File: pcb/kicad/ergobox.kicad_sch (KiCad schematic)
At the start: 1 part

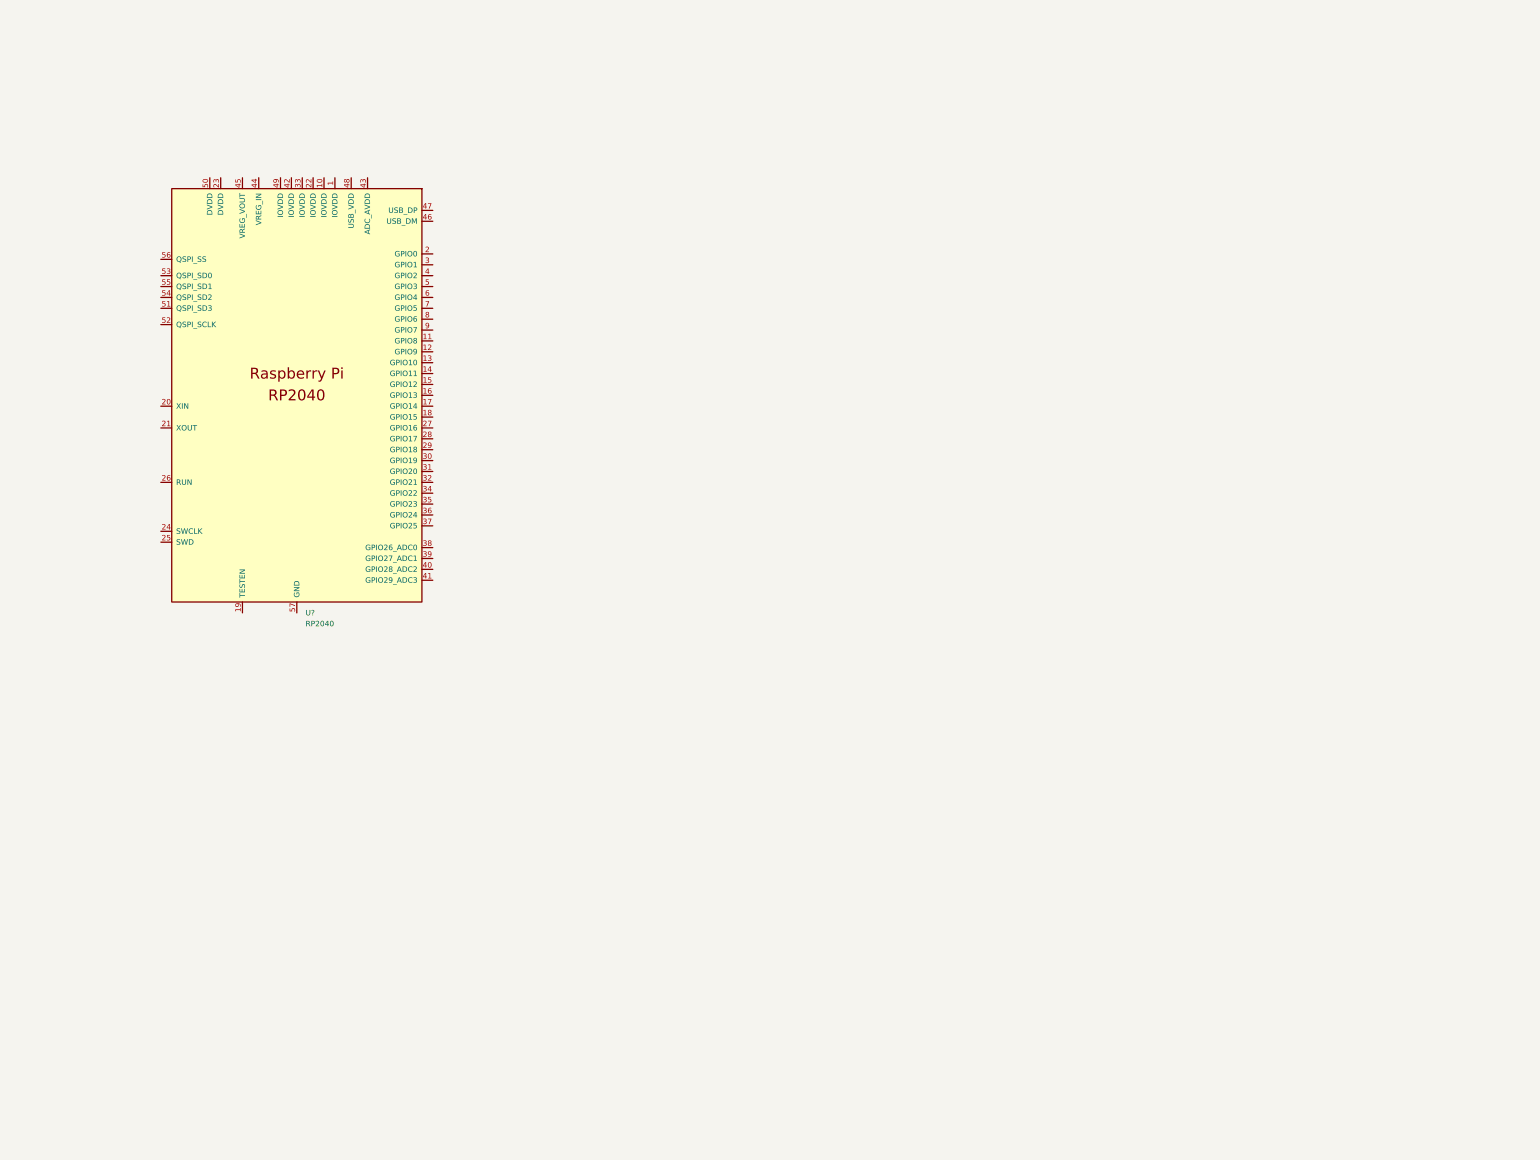
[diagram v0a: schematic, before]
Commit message: feat: adds initial schematic design
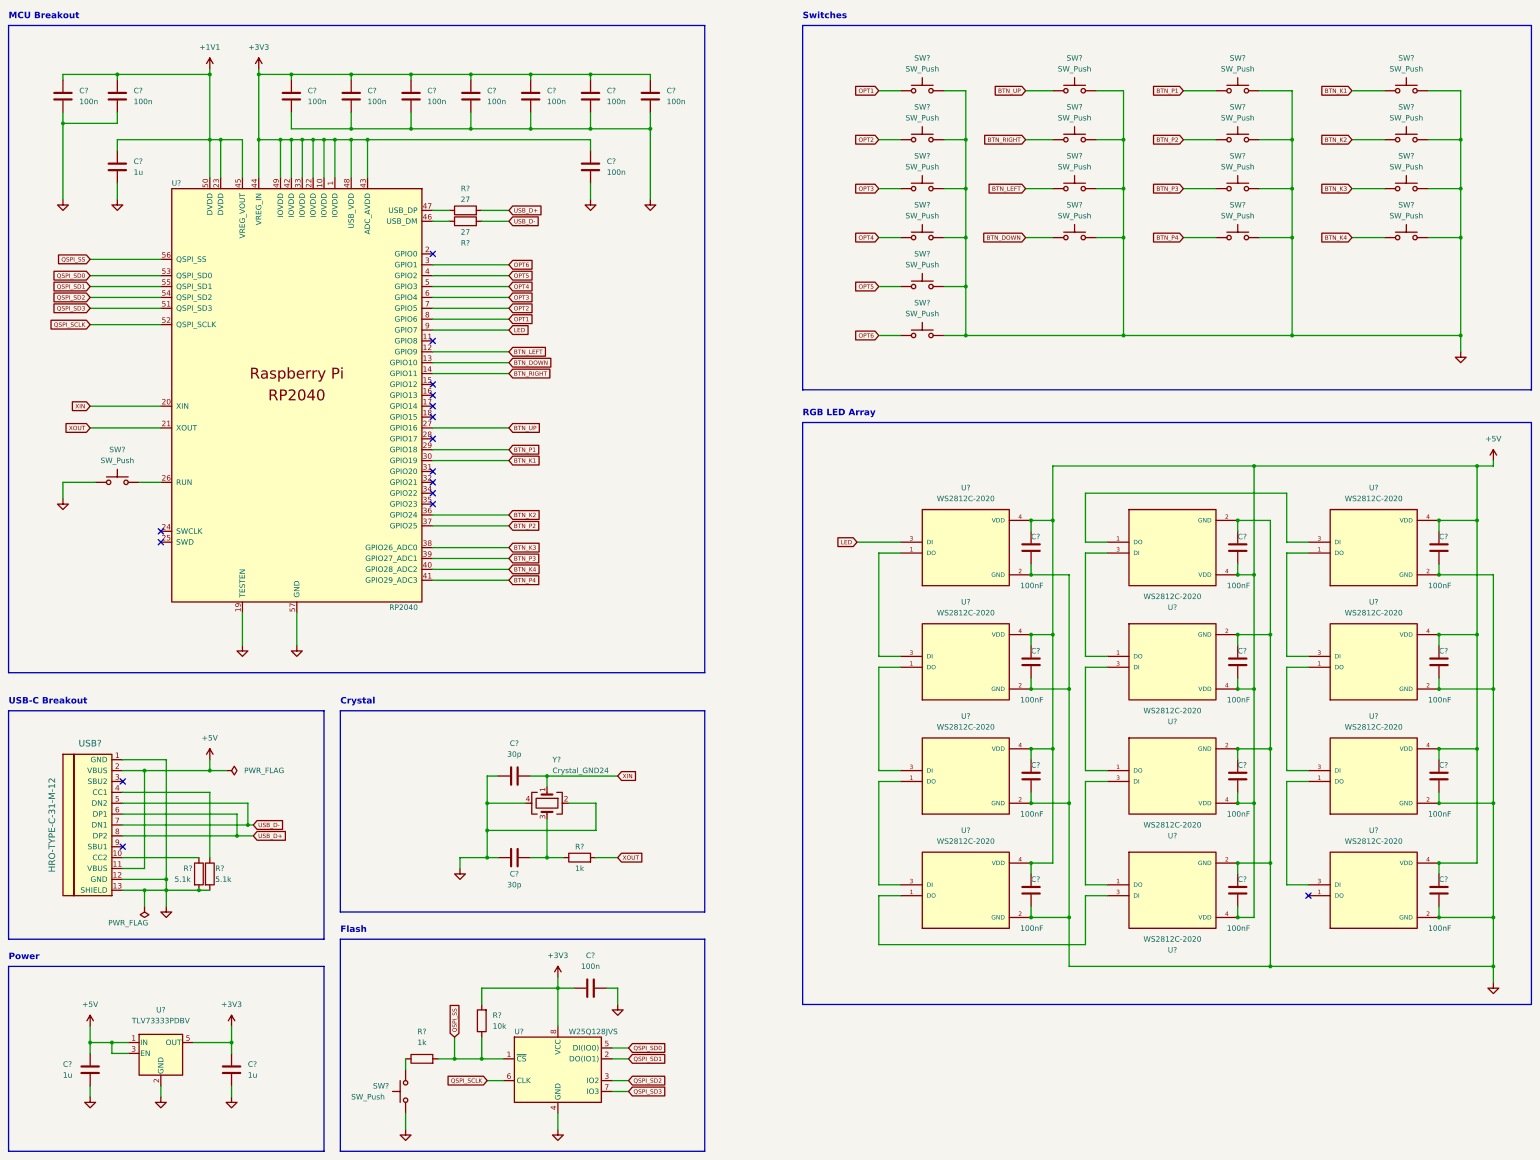
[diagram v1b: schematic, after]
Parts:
- added C? (x11): 100n, symbol Device:C
- added C? (x12): 100nF, symbol Device:C
- added C? (x3): 1u, symbol Device:C
- added C? (x2): 30p, symbol Device:C
- added R? (x2): 5.1k, symbol Device:R
- added R? (x2): 1k, symbol Device:R
- added R?: 10k, symbol Device:R
- added R? (x2): 27, symbol Device:R
- added SW? (x20): SW_Push, symbol Switch:SW_Push
- added U? (x12): WS2812C-2020, LED_WS2812C-2020, symbol WS2812C-2020:WS2812C-2020
- added U?: W25Q128JVS, Package_SO:SOIC-8_5.23x5.23mm_P1.27mm, symbol Memory_Flash:W25Q128JVS
- added U?: TLV73333PDBV, Package_TO_SOT_SMD:SOT-23-5, symbol Regulator_Linear:TLV73333PDBV
- added USB?: HRO-TYPE-C-31-M-12, symbol USB-C:HRO-TYPE-C-31-M-12
- added Y?: Crystal_GND24, symbol Device:Crystal_GND24
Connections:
- net +3V3: now reaches U?.1 (IOVDD)
- net +3V3: now also U?.10 (IOVDD), U?.22 (IOVDD), U?.33 (IOVDD), U?.42 (IOVDD), U?.43 (ADC_AVDD), U?.44 (VREG_IN), U?.48 (USB_VDD), U?.49 (IOVDD), C?.1, C?.1, C?.1, C?.1, C?.1, C?.1, C?.1, C?.1, C?.1, C?.1, R?.2, U?.5 (OUT), U?.8 (VCC)
- net BTN_LEFT: now reaches U?.12 (GPIO9)
- net BTN_LEFT: now also SW?.1
- net BTN_DOWN: now reaches U?.13 (GPIO10)
- net BTN_DOWN: now also SW?.1
- net BTN_RIGHT: now reaches U?.14 (GPIO11)
- net BTN_RIGHT: now also SW?.1
- net GND: now reaches U?.19 (TESTEN)
- net GND: now also U?.57 (GND), C?.1, C?.1, C?.1, C?.1, C?.1, C?.1, C?.2, C?.2, C?.2, C?.2, C?.2, C?.2, C?.2, C?.2, C?.2, C?.2, C?.2, C?.2, C?.2, C?.2, C?.2, C?.2, C?.2, C?.2, C?.2, C?.2, C?.2, C?.2, R?.2, R?.2, SW?.1, SW?.1, SW?.2, SW?.2, SW?.2, SW?.2, SW?.2, SW?.2, SW?.2, SW?.2, SW?.2, SW?.2, SW?.2, SW?.2, SW?.2, SW?.2, SW?.2, SW?.2, SW?.2, SW?.2, U?.2 (GND), U?.2 (GND), U?.2 (GND), U?.2 (GND), U?.2 (GND), U?.2 (GND), U?.2 (GND), U?.2 (GND), U?.2 (GND), U?.2 (GND), U?.2 (GND), U?.2 (GND), U?.2 (GND), U?.4 (GND), USB?.1 (GND), USB?.12 (GND), USB?.13 (SHIELD), Y?.2, Y?.4
- net XIN: now reaches U?.20 (XIN)
- net XIN: now also C?.2, Y?.1
- net XOUT: now reaches U?.21 (XOUT)
- net XOUT: now also R?.2
- net +1V1: now reaches U?.23 (DVDD)
- net +1V1: now also U?.45 (VREG_VOUT), U?.50 (DVDD), C?.1, C?.1, C?.1
- net at U?.26 (RUN): now also SW?.2
- net BTN_UP: now reaches U?.27 (GPIO16)
- net BTN_UP: now also SW?.1
- net BTN_P1: now reaches U?.29 (GPIO18)
- net BTN_P1: now also SW?.1
- net OPT6: now reaches U?.3 (GPIO1)
- net OPT6: now also SW?.1
- net BTN_K1: now reaches U?.30 (GPIO19)
- net BTN_K1: now also SW?.1
- net BTN_K2: now reaches U?.36 (GPIO24)
- net BTN_K2: now also SW?.1
- net BTN_P2: now reaches U?.37 (GPIO25)
- net BTN_P2: now also SW?.1
- net BTN_K3: now reaches U?.38 (GPIO26_ADC0)
- net BTN_K3: now also SW?.1
- net BTN_P3: now reaches U?.39 (GPIO27_ADC1)
- net BTN_P3: now also SW?.1
- net OPT5: now reaches U?.4 (GPIO2)
- net OPT5: now also SW?.1
- net BTN_K4: now reaches U?.40 (GPIO28_ADC2)
- net BTN_K4: now also SW?.1
- net BTN_P4: now reaches U?.41 (GPIO29_ADC3)
- net BTN_P4: now also SW?.1
- net at U?.46 (USB_DM): now also R?.1
- net at U?.47 (USB_DP): now also R?.1
- net OPT4: now reaches U?.5 (GPIO3)
- net OPT4: now also SW?.1
- net QSPI_SD3: now reaches U?.51 (QSPI_SD3)
- net QSPI_SD3: now also U?.7 (IO3)
- net QSPI_SCLK: now reaches U?.52 (QSPI_SCLK)
- net QSPI_SCLK: now also U?.6 (CLK)
- net QSPI_SD0: now reaches U?.53 (QSPI_SD0)
- net QSPI_SD0: now also U?.5 (DI(IO0))
- net QSPI_SD2: now reaches U?.54 (QSPI_SD2)
- net QSPI_SD2: now also U?.3 (IO2)
- net QSPI_SD1: now reaches U?.55 (QSPI_SD1)
- net QSPI_SD1: now also U?.2 (DO(IO1))
- net QSPI_SS: now reaches U?.56 (QSPI_SS)
- net QSPI_SS: now also R?.1, R?.2, U?.1 (~{CS})
- net OPT3: now reaches U?.6 (GPIO4)
- net OPT3: now also SW?.1
- net OPT2: now reaches U?.7 (GPIO5)
- net OPT2: now also SW?.1
- net OPT1: now reaches U?.8 (GPIO6)
- net OPT1: now also SW?.1
- net LED: now reaches U?.9 (GPIO7)
- net LED: now also U?.3 (DI)
- new net: R?.1, USB?.10 (CC2)
- new net: U?.1 (DO), U?.3 (DI) (x11)
- new net: R?.1, USB?.4 (CC1)
- new net: C?.2, R?.1, Y?.3
- new net: R?.1, SW?.2
- new net +5V: C?.1, C?.1, C?.1, C?.1, C?.1, C?.1, C?.1, C?.1, C?.1, C?.2, C?.2, C?.2, C?.2, U?.1 (IN), U?.3 (EN), U?.4 (VDD), U?.4 (VDD), U?.4 (VDD), U?.4 (VDD), U?.4 (VDD), U?.4 (VDD), U?.4 (VDD), U?.4 (VDD), U?.4 (VDD), U?.4 (VDD), U?.4 (VDD), U?.4 (VDD), USB?.11 (VBUS), USB?.2 (VBUS)
- new net USB_D+: R?.2, USB?.6 (DP1), USB?.8 (DP2)
- new net USB_D-: R?.2, USB?.5 (DN2), USB?.7 (DN1)
- no-connect marks 0 -> 16
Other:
- note added: "Crystal"
- note added: "Flash"
- note added: "MCU Breakout"
- note added: "Power"
- note added: "RGB LED Array"
- note added: "Switches"
- note added: "USB-C Breakout"
- company: (none) -> techlifemusic

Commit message: feat: updates footprints for Kailh switches and WS2812C-2020
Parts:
- D1, D10, D11, D12, D2, D3, D4, D5, D6, D7, D8, D9: renamed from U?; footprint LED_WS2812C-2020 -> WS2812C-2020:LED_WS2812C-2020
- SW10, SW11, SW12, SW13, SW14, SW15, SW16, SW17, SW18, SW19, SW20, SW9: renamed from SW?; value SW_Push -> Kailh; footprint (none) -> Keyswitches:Kailh_socket_PG1350
- USB1: renamed from USB?; footprint (none) -> USB-C:HRO-TYPE-C-31-M-12
- gave numbers to parts that had none: 47
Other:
- title: Ergobox RGB Fight Controller -> Ergobox

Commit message: feat: adds footprints to remaining components
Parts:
- C1, C10, C11, C12, C13, C14, C15, C16, C17, C18, C19, C2, C20, C21, C22, C23, C24, C25, C26, C27, C28, C3, C4, C5, C6, C7, C8, C9: footprint (none) -> Capacitor_SMD:C_0402_1005Metric
- R1, R2, R3, R4, R5, R6, R7: footprint (none) -> Resistor_SMD:R_0402_1005Metric
- SW1, SW2: footprint (none) -> Button_Switch_SMD:SW_SPST_Omron_B3FS-100xP
- SW3, SW4, SW5, SW6, SW7, SW8: footprint (none) -> Button_Switch_THT:SW_PUSH_6mm_H5mm
- Y1: footprint (none) -> Crystal:Crystal_SMD_3225-4Pin_3.2x2.5mm

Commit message: refactor: changes footprint for Kailh switches to 1350_optional
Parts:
- SW10, SW11, SW12, SW13, SW14, SW15, SW16, SW17, SW18, SW19, SW20, SW9: footprint Keyswitches:Kailh_socket_PG1350 -> Keyswitches:Kailh_socket_PG1350_optional
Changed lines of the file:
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@@
     (property "Reference" "SW11" (id 0) (at 266.7 50.8 0))
     (property "Value" "Kailh" (id 1) (at 266.7 53.34 0))
-    (property "Footprint" "Keyswitches:Kailh_socket_PG1350" (id 2) (at 266.7 53.34 0)
+    (property "Footprint" "Keyswitches:Kailh_socket_PG1350_optional" (id 2) (at 266.7 53.34 0)
       (effects (font (size 1.27 1.27)) hide)
     )
@@
     (property "Reference" "SW17" (id 0) (at 344.17 27.94 0))
     (property "Value" "Kailh" (id 1) (at 344.17 30.48 0))
-    (property "Footprint" "Keyswitches:Kailh_socket_PG1350" (id 2) (at 344.17 30.48 0)
+    (property "Footprint" "Keyswitches:Kailh_socket_PG1350_optional" (id 2) (at 344.17 30.48 0)
       (effects (font (size 1.27 1.27)) hide)
     )
@@
     (property "Reference" "SW16" (id 0) (at 304.8 62.23 0))
     (property "Value" "Kailh" (id 1) (at 304.8 64.77 0))
-    (property "Footprint" "Keyswitches:Kailh_socket_PG1350" (id 2) (at 304.8 64.77 0)
+    (property "Footprint" "Keyswitches:Kailh_socket_PG1350_optional" (id 2) (at 304.8 64.77 0)
       (effects (font (size 1.27 1.27)) hide)
     )
@@
     (property "Reference" "SW12" (id 0) (at 266.7 62.23 0))
     (property "Value" "Kailh" (id 1) (at 266.7 64.77 0))
-    (property "Footprint" "Keyswitches:Kailh_socket_PG1350" (id 2) (at 266.7 64.77 0)
+    (property "Footprint" "Keyswitches:Kailh_socket_PG1350_optional" (id 2) (at 266.7 64.77 0)
       (effects (font (size 1.27 1.27)) hide)
     )
@@
     (property "Reference" "SW14" (id 0) (at 304.8 39.37 0))
     (property "Value" "Kailh" (id 1) (at 304.8 41.91 0))
-    (property "Footprint" "Keyswitches:Kailh_socket_PG1350" (id 2) (at 304.8 41.91 0)
+    (property "Footprint" "Keyswitches:Kailh_socket_PG1350_optional" (id 2) (at 304.8 41.91 0)
       (effects (font (size 1.27 1.27)) hide)
     )
@@
     (property "Reference" "SW20" (id 0) (at 344.17 62.23 0))
     (property "Value" "Kailh" (id 1) (at 344.17 64.77 0))
-    (property "Footprint" "Keyswitches:Kailh_socket_PG1350" (id 2) (at 344.17 64.77 0)
+    (property "Footprint" "Keyswitches:Kailh_socket_PG1350_optional" (id 2) (at 344.17 64.77 0)
       (effects (font (size 1.27 1.27)) hide)
     )
@@
     (property "Reference" "SW10" (id 0) (at 266.7 39.37 0))
     (property "Value" "Kailh" (id 1) (at 266.7 41.91 0))
-    (property "Footprint" "Keyswitches:Kailh_socket_PG1350" (id 2) (at 266.7 41.91 0)
+    (property "Footprint" "Keyswitches:Kailh_socket_PG1350_optional" (id 2) (at 266.7 41.91 0)
       (effects (font (size 1.27 1.27)) hide)
     )
@@
     (property "Reference" "SW19" (id 0) (at 344.17 50.8 0))
     (property "Value" "Kailh" (id 1) (at 344.17 53.34 0))
-    (property "Footprint" "Keyswitches:Kailh_socket_PG1350" (id 2) (at 344.17 53.34 0)
+    (property "Footprint" "Keyswitches:Kailh_socket_PG1350_optional" (id 2) (at 344.17 53.34 0)
       (effects (font (size 1.27 1.27)) hide)
     )
@@
     (property "Reference" "SW18" (id 0) (at 344.17 39.37 0))
     (property "Value" "Kailh" (id 1) (at 344.17 41.91 0))
-    (property "Footprint" "Keyswitches:Kailh_socket_PG1350" (id 2) (at 344.17 41.91 0)
+    (property "Footprint" "Keyswitches:Kailh_socket_PG1350_optional" (id 2) (at 344.17 41.91 0)
       (effects (font (size 1.27 1.27)) hide)
     )
@@
     (property "Reference" "SW15" (id 0) (at 304.8 50.8 0))
     (property "Value" "Kailh" (id 1) (at 304.8 53.34 0))
-    (property "Footprint" "Keyswitches:Kailh_socket_PG1350" (id 2) (at 304.8 53.34 0)
+    (property "Footprint" "Keyswitches:Kailh_socket_PG1350_optional" (id 2) (at 304.8 53.34 0)
       (effects (font (size 1.27 1.27)) hide)
     )
@@
     (property "Reference" "SW9" (id 0) (at 266.7 27.94 0))
     (property "Value" "Kailh" (id 1) (at 266.7 30.48 0))
-    (property "Footprint" "Keyswitches:Kailh_socket_PG1350" (id 2) (at 266.7 30.48 0)
+    (property "Footprint" "Keyswitches:Kailh_socket_PG1350_optional" (id 2) (at 266.7 30.48 0)
       (effects (font (size 1.27 1.27)) hide)
     )
@@
     (property "Reference" "SW13" (id 0) (at 304.8 27.94 0))
     (property "Value" "Kailh" (id 1) (at 304.8 30.48 0))
-    (property "Footprint" "Keyswitches:Kailh_socket_PG1350" (id 2) (at 304.8 30.48 0)
+    (property "Footprint" "Keyswitches:Kailh_socket_PG1350_optional" (id 2) (at 304.8 30.48 0)
       (effects (font (size 1.27 1.27)) hide)
     )
@@
     )
     (path "/e7e50001-1420-4b1c-9a9c-244be6cee891"
-      (reference "SW9") (unit 1) (value "Kailh") (footprint "Keyswitches:Kailh_socket_PG1350")
+      (reference "SW9") (unit 1) (value "Kailh") (footprint "Keyswitches:Kailh_socket_PG1350_optional")
     )
     (path "/6ffa2bda-adb8-4b45-b2f3-66d14af70739"
-      (reference "SW10") (unit 1) (value "Kailh") (footprint "Keyswitches:Kailh_socket_PG1350")
+      (reference "SW10") (unit 1) (value "Kailh") (footprint "Keyswitches:Kailh_socket_PG1350_optional")
     )
     (path "/0d5161b8-5c58-4924-99b4-8ca9b7edfc0a"
-      (reference "SW11") (unit 1) (value "Kailh") (footprint "Keyswitches:Kailh_socket_PG1350")
+      (reference "SW11") (unit 1) (value "Kailh") (footprint "Keyswitches:Kailh_socket_PG1350_optional")
     )
     (path "/4a2c44e2-5354-4d12-93e7-55de66eaf6db"
-      (reference "SW12") (unit 1) (value "Kailh") (footprint "Keyswitches:Kailh_socket_PG1350")
+      (reference "SW12") (unit 1) (value "Kailh") (footprint "Keyswitches:Kailh_socket_PG1350_optional")
     )
     (path "/f782518d-1e58-45b8-86df-64b2f301f57b"
-      (reference "SW13") (unit 1) (value "Kailh") (footprint "Keyswitches:Kailh_socket_PG1350")
+      (reference "SW13") (unit 1) (value "Kailh") (footprint "Keyswitches:Kailh_socket_PG1350_optional")
     )
     (path "/53fbce93-16c6-4ed7-9a04-6a5f272cab51"
-      (reference "SW14") (unit 1) (value "Kailh") (footprint "Keyswitches:Kailh_socket_PG1350")
+      (reference "SW14") (unit 1) (value "Kailh") (footprint "Keyswitches:Kailh_socket_PG1350_optional")
     )
     (path "/d72db84b-8b36-4381-8bae-7e7b8e71a550"
-      (reference "SW15") (unit 1) (value "Kailh") (footprint "Keyswitches:Kailh_socket_PG1350")
+      (reference "SW15") (unit 1) (value "Kailh") (footprint "Keyswitches:Kailh_socket_PG1350_optional")
     )
     (path "/2d890ef2-4562-41a2-a026-1abb741422ac"
-      (reference "SW16") (unit 1) (value "Kailh") (footprint "Keyswitches:Kailh_socket_PG1350")
+      (reference "SW16") (unit 1) (value "Kailh") (footprint "Keyswitches:Kailh_socket_PG1350_optional")
     )
     (path "/19b0ce15-4c08-412b-87c9-e357c06d1577"
-      (reference "SW17") (unit 1) (value "Kailh") (footprint "Keyswitches:Kailh_socket_PG1350")
+      (reference "SW17") (unit 1) (value "Kailh") (footprint "Keyswitches:Kailh_socket_PG1350_optional")
     )
     (path "/bf14133a-e3dd-4876-94ab-bfabcac675ee"
-      (reference "SW18") (unit 1) (value "Kailh") (footprint "Keyswitches:Kailh_socket_PG1350")
+      (reference "SW18") (unit 1) (value "Kailh") (footprint "Keyswitches:Kailh_socket_PG1350_optional")
     )
     (path "/b30149f7-7340-4a08-a501-4fd458ccf120"
-      (reference "SW19") (unit 1) (value "Kailh") (footprint "Keyswitches:Kailh_socket_PG1350")
+      (reference "SW19") (unit 1) (value "Kailh") (footprint "Keyswitches:Kailh_socket_PG1350_optional")
     )
     (path "/677ff06d-f79f-4636-ba21-beec29f993c2"
-      (reference "SW20") (unit 1) (value "Kailh") (footprint "Keyswitches:Kailh_socket_PG1350")
+      (reference "SW20") (unit 1) (value "Kailh") (footprint "Keyswitches:Kailh_socket_PG1350_optional")
     )
     (path "/fe9c4ac9-a70d-46e0-af36-a86bcd3800dd"
